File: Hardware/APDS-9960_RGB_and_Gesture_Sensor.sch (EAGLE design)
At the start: 18 parts, among them U1 APDS-9960

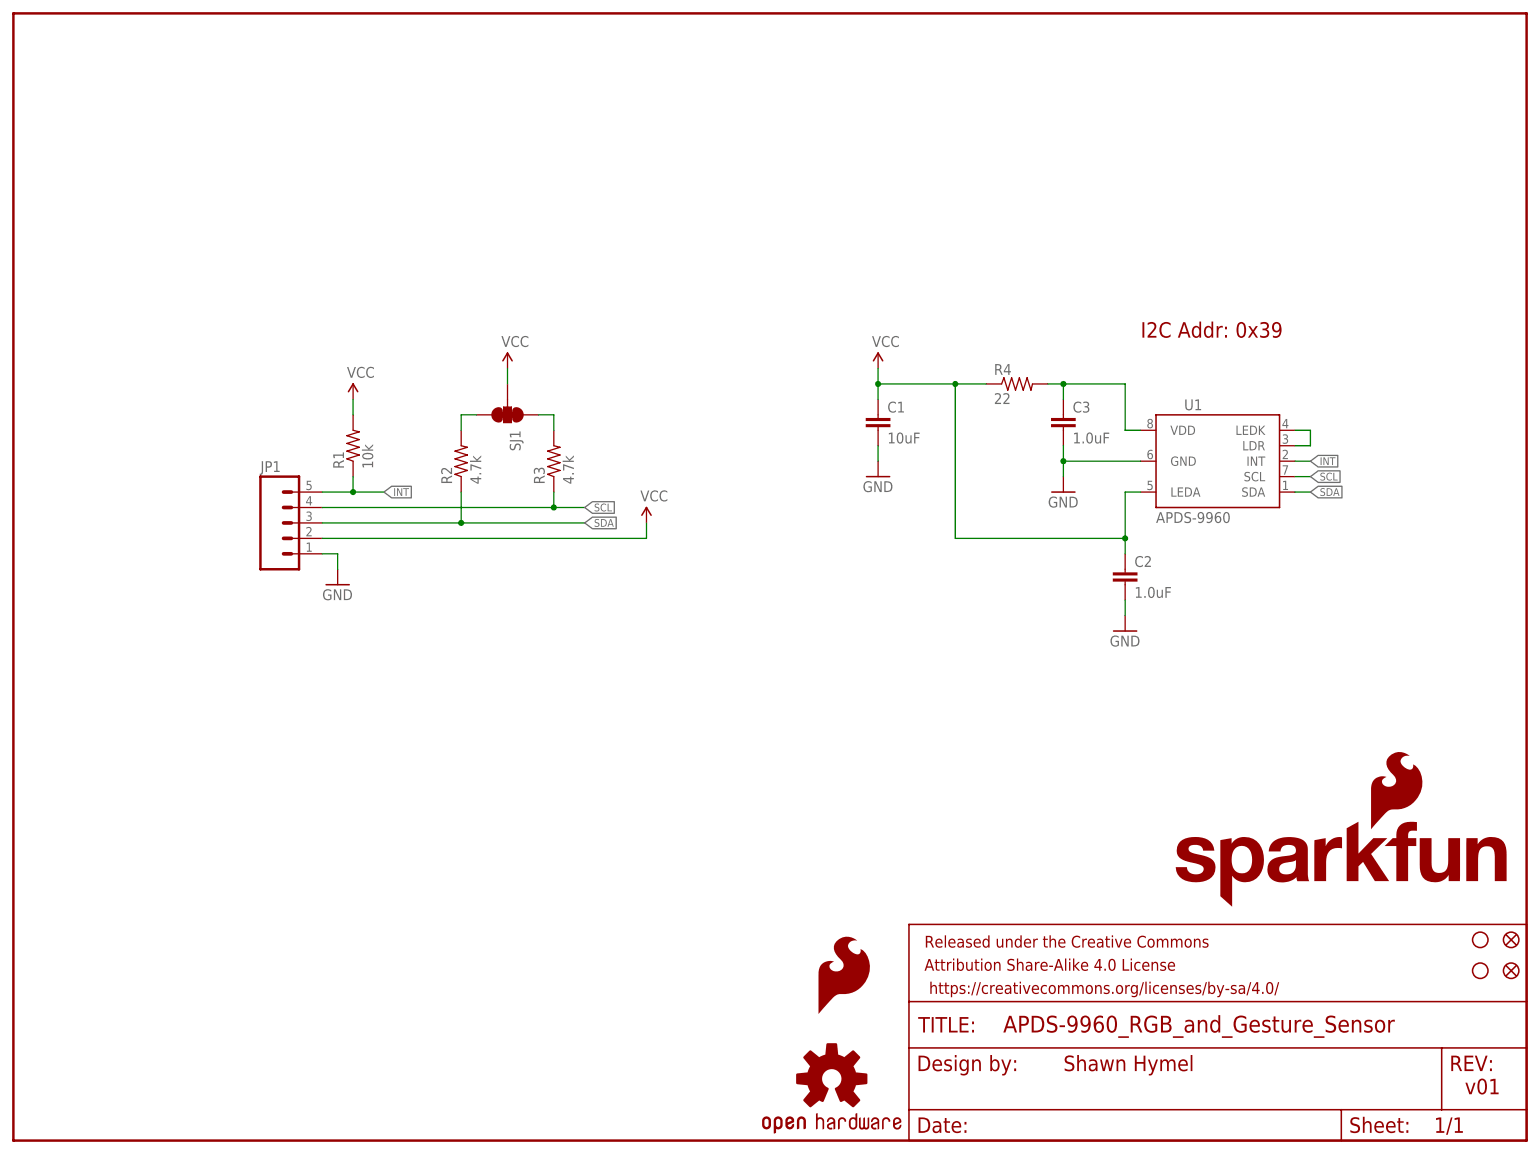
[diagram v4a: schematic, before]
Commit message: Added separate VLED (VL) pin, connected VL and VCC with solder jumper and optional resistor. Re-did layout to support new features.
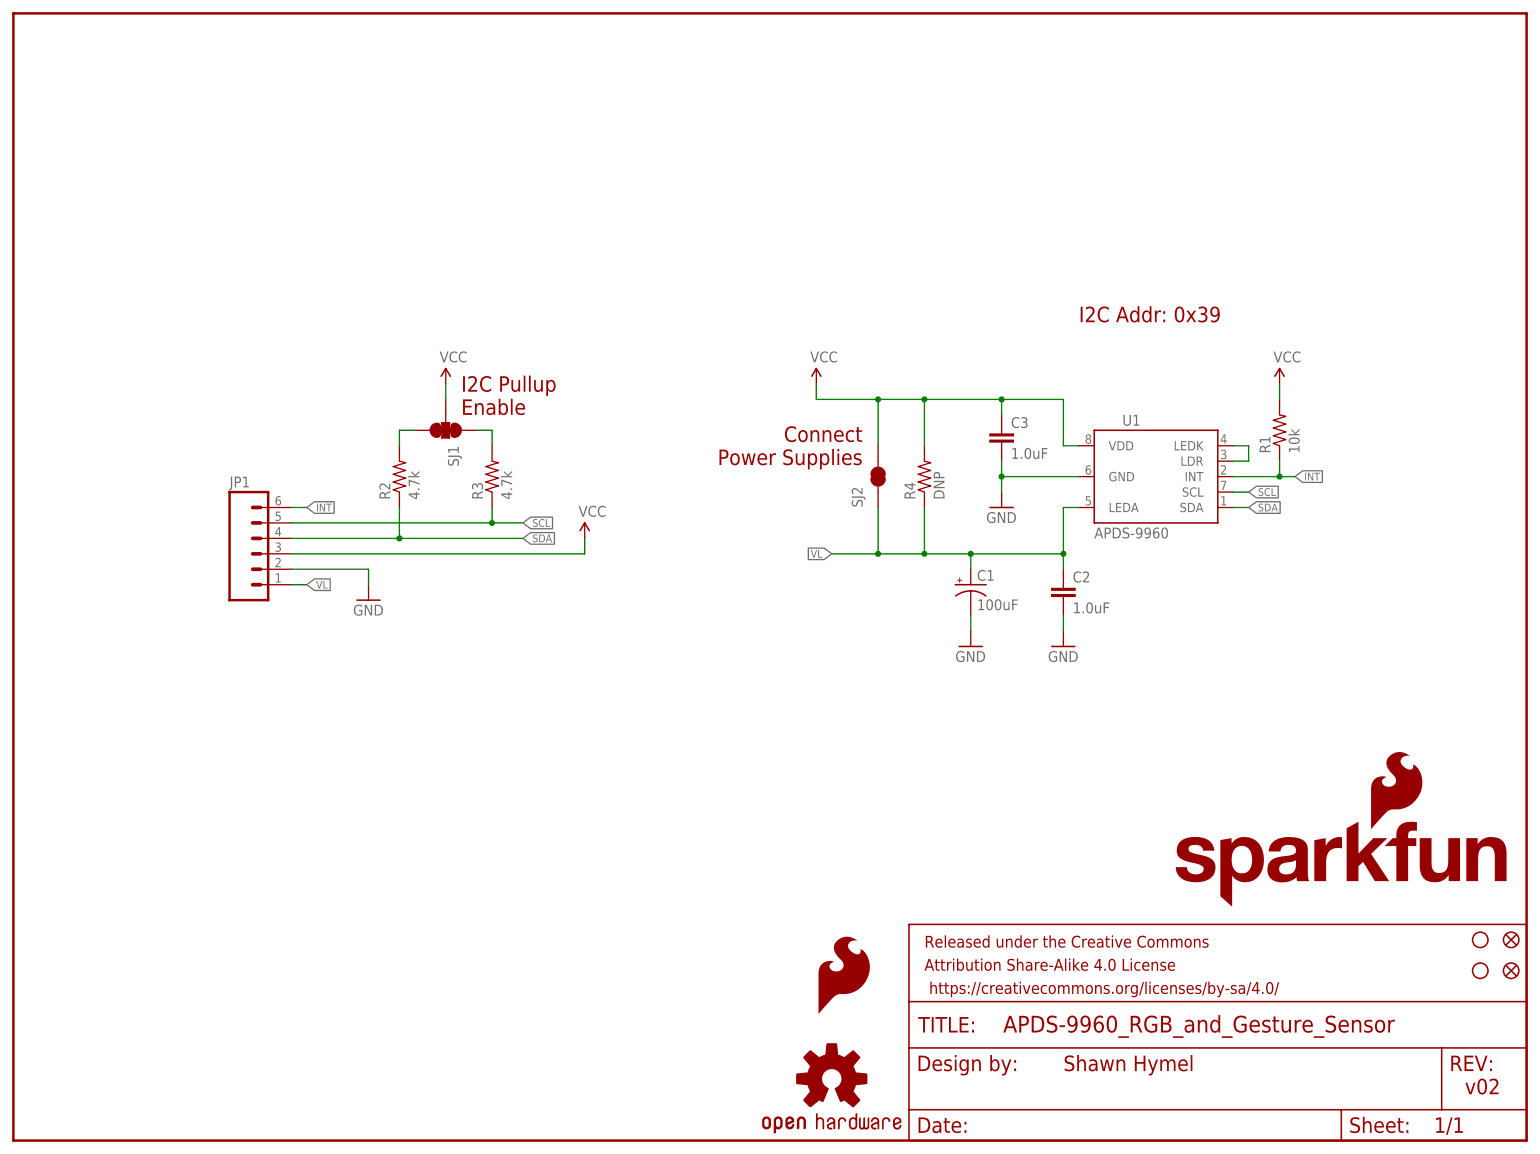
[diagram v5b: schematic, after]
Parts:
- added SJ2: SOLDERJUMPERNC, SparkFun-Retired:SOLDERJUMPERNC
- C1: value 10uF -> 100uF; device SparkFun-Capacitors:10UF50V20%(1210) -> SparkFun-Capacitors:100UF-10V-10%(TANT)
- JP1: device SparkFun-Connectors:M05PTH -> SparkFun-Connectors:M06SIP
- R4: value 22 -> DNP; device SparkFun-Resistors:22OHM1/10W1%(0603) -> SparkFun-Resistors:RESISTOR0603
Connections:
- removed net N$3: C3.1, R4.2, U1.VDD
- new net VL: C1.+, C2.1, JP1.1, R4.1, SJ2.1, U1.LEDA
- net GND: now also C1.-, JP1.2; no longer C1.2, JP1.1
- net INT: now also JP1.6; no longer JP1.5
- net SCL: now also JP1.5; no longer JP1.4
- net SDA: now also JP1.4; no longer JP1.3
- net VCC: now also C3.1, JP1.3, R4.2, SJ2.2, U1.VDD; no longer C1.1, C2.1, JP1.2, R4.1, U1.LEDA
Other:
- note added: "Connect Power Supplies"
- note added: "I2C Pullup Enable"
- note added: "v02"
- note removed: "v01"
- moved on the sheet: C2, C3, R1, R2, R3, R4, SJ1, U1
